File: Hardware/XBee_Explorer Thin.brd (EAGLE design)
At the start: 43.2 x 52.1 mm, 65 parts, among them J4 QWIIC_RIGHT_ANGLE, Q2 3.1A/30V/105mΩ, U1 FSUSB30MUX_MSOP10, U2 AP63203, U3 ESD Diode, U5 ESD Diode, U6 CP210X

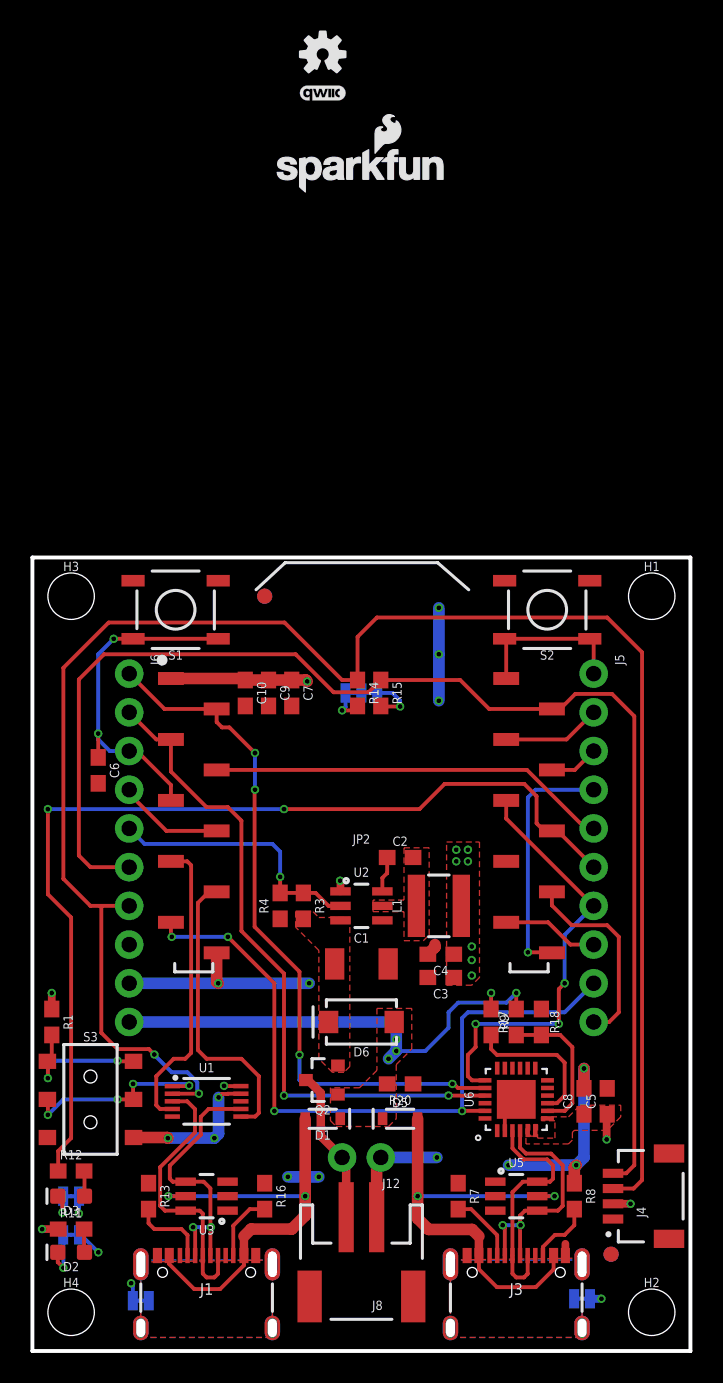
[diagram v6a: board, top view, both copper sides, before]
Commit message: Adds labels
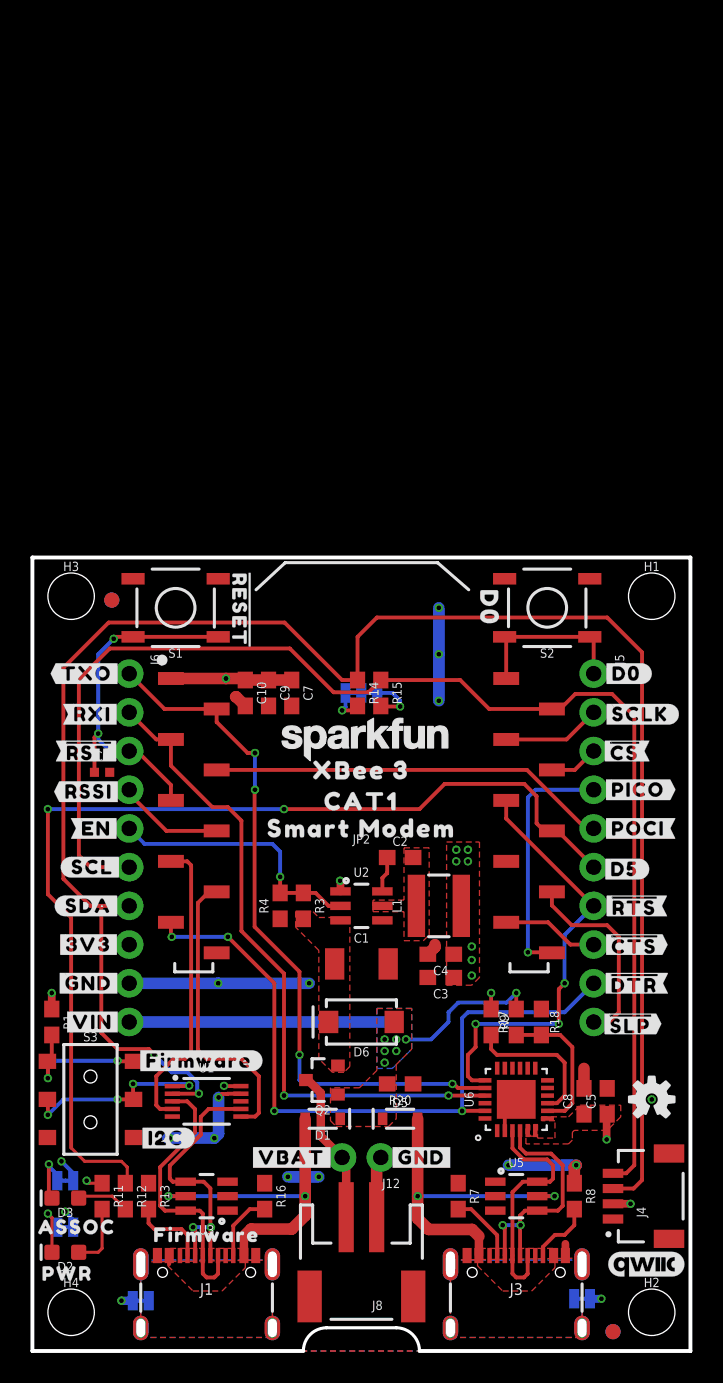
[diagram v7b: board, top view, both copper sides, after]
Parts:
- removed JP1, JP3: JUMPER-SMT_2_NC_TRACE_SILK, SparkFun-Jumpers:SMT-JUMPER_2_NC_TRACE_SILK
- added ALED, PLED: JUMPER-SMT_2_NC_TRACE_SILK, SparkFun-Jumpers:SMT-JUMPER_2_NC_TRACE_SILK
- added U$1: (no value), top:#RXI#14
- added U$10: (no value), top:#D0#18
- added U$11, U$37: (no value), top:#VBAT#5
- added U$12: (no value), top:#D3#AD3#22
- added U$13: (no value), top:#D4#PICO#24
- added U$14: (no value), top:#D12#POCI#23
- added U$15: (no value), top:#TXO#D13#13
- added U$16: (no value), top:#RXI#D14#15
- added U$17, U$2: (no value), top:##RST##15
- added U$18: (no value), top:#RSSI#D10#17
- added U$19: (no value), top:#AD1#D1#7
- added U$20, U$25, U$38, U$45: (no value), top:#GND#0
- added U$21, U$24: (no value), top:#EN#17
- added U$22: (no value), top:#SDA#D11#8
- added U$23, U$53: (no value), top:XBEE_335
- added U$26: (no value), top:#I2C#33
- added U$27: (no value), top:#ALED#21
- added U$28: (no value), top:#PICO#21
- added U$29: (no value), top:#POCI#20
- added U$3: (no value), top:##CS##19
- added U$30: (no value), top:#RESET#28
- added U$31: (no value), top:#RSSI#16
- added U$32: (no value), top:#SCL#6
- added U$33: (no value), top:#SCLK#18
- added U$34: (no value), top:#SDA#7
- added U$35: (no value), top:#SHLD#30
- added U$36: (no value), top:#SHLD1#31
- added U$39: (no value), bot:#D5#3
- added U$4: (no value), top:##CTS##23
- added U$40: (no value), bot:D03
- added U$41, U$46: (no value), top:#VIN#4
- added U$42: (no value), top:PWR26
- added U$43: (no value), top:ASSOC27
- added U$44, U$9: (no value), top:#3V3#1
- added U$47: (no value), top:##SLP##25
- added U$48: (no value), bot:#FIRMWARE#31
- added U$49: (no value), bot:#I2C#31
- added U$5: (no value), top:##DTR##24
- added U$50: (no value), top:#TXO#12
- added U$51: (no value), top:SMART_MODEM1337
- added U$52, U$61: (no value), top:CAT1336
- added U$54: (no value), top:#PLED#20
- added U$55: (no value), top:#D0#AD0#18
- added U$56: (no value), top:#D5#ASSOC#24
- added U$57: (no value), top:#D6##RTS##24
- added U$58: (no value), top:#D7##CTS##25
- added U$59: (no value), top:#D8##DTR##26
- added U$6: (no value), top:#D2#AD2#19
- added U$60: (no value), top:#D9##SLP##27
- added U$62: (no value), top:SMART1337
- added U$63: (no value), SparkFun-Aesthetics:SFE_LOGO_NAME_.1
- added U$64: (no value), top:MODEM1338
- added U$7: (no value), top:##RTS##22
- added U$8: (no value), top:FIRMWARE29
- C6: device SparkFun-Capacitors:0603 -> SparkFun-Capacitors:0402-TIGHT
- LOGO1: value SFE_LOGO_NAME_FLAME.1_INCH -> SFE_LOGO_NAME.1_INCH; device SparkFun-Aesthetics:SFE_LOGO_NAME_FLAME_.1 -> SparkFun-Aesthetics:SFE_LOGO_NAME_.1
- LOGO3: value QWIIC_LOGO_3MM -> QWIIC_LOGO_5MM; device SparkFun-Aesthetics:QWIIC_3MM -> SparkFun-Aesthetics:QWIIC_5MM
- moved LOGO3 79.7 mm to (40.3, 5.71)
- moved LOGO2 71.9 mm to (40.6, 16.5)
- moved LOGO1 37.3 mm to (21.8, 40.1)
- moved FD1 10.0 mm to (5.21, 49.3)
- moved FD2 10.0 mm to (5.21, 49.3)
- moved FD3 5.08 mm to (38.1, 1.27)
- moved FD4 5.08 mm to (38.1, 1.27)
- moved R12 3.92 mm to (6.10, 10.2), turned to 270 degrees
- moved R11 2.96 mm to (4.57, 10.2), turned to 270 degrees
- moved D3 0.40 mm to (2.16, 10.0)
- moved D2 0.38 mm to (2.16, 6.48)
- moved C6 0.28 mm to (4.57, 38.0), turned to 0 degrees
- moved S1 0.13 mm to (9.40, 48.8)
- moved S2 0.13 mm to (33.8, 48.8)
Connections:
- net GND: now also ALED.1, PLED.1; no longer JP1.1, JP3.1
- net N$21: now also ALED.2; no longer JP3.2
- net N$23: now also PLED.2; no longer JP1.2
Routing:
- net GND: track 61.8 -> 47.6 mm, vias 18 -> 17
- net V_USB: track 30.1 -> 22.4 mm
- net V_USB_2: track 29.8 -> 22.9 mm
- net VIN: track 31.0 -> 27.1 mm, vias 4 -> 7
- net D5/ASSOCIATE: track 64.5 -> 68.0 mm
- net N$7: track 1.54 -> 4.22 mm
- net N$12: track 1.66 -> 3.46 mm
- net N$21: track 2.31 -> 3.62 mm
- net !RESET!: track 22.5 -> 23.6 mm
- net 3.3V: track 16.8 -> 15.8 mm
- net N$23: track 3.33 -> 4.08 mm
- added copper zone on layer 16, net VIN
- added copper zone on layer 1, net V_USB
- added copper zone on layer 1, net V_USB_2
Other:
- outline, holes or cut-outs redrawn

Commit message: Adds version
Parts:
- moved S2 0.51 mm to (34.3, 48.8)
- moved S1 0.51 mm to (8.89, 48.8)
- moved U$40 0.40 mm to (30.4, 48.6)
- moved U$30 0.38 mm to (13.3, 48.6)
- renumbered JP2 to J2
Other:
- board text added: "v01"
